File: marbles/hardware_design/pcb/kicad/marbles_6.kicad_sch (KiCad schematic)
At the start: 22 parts

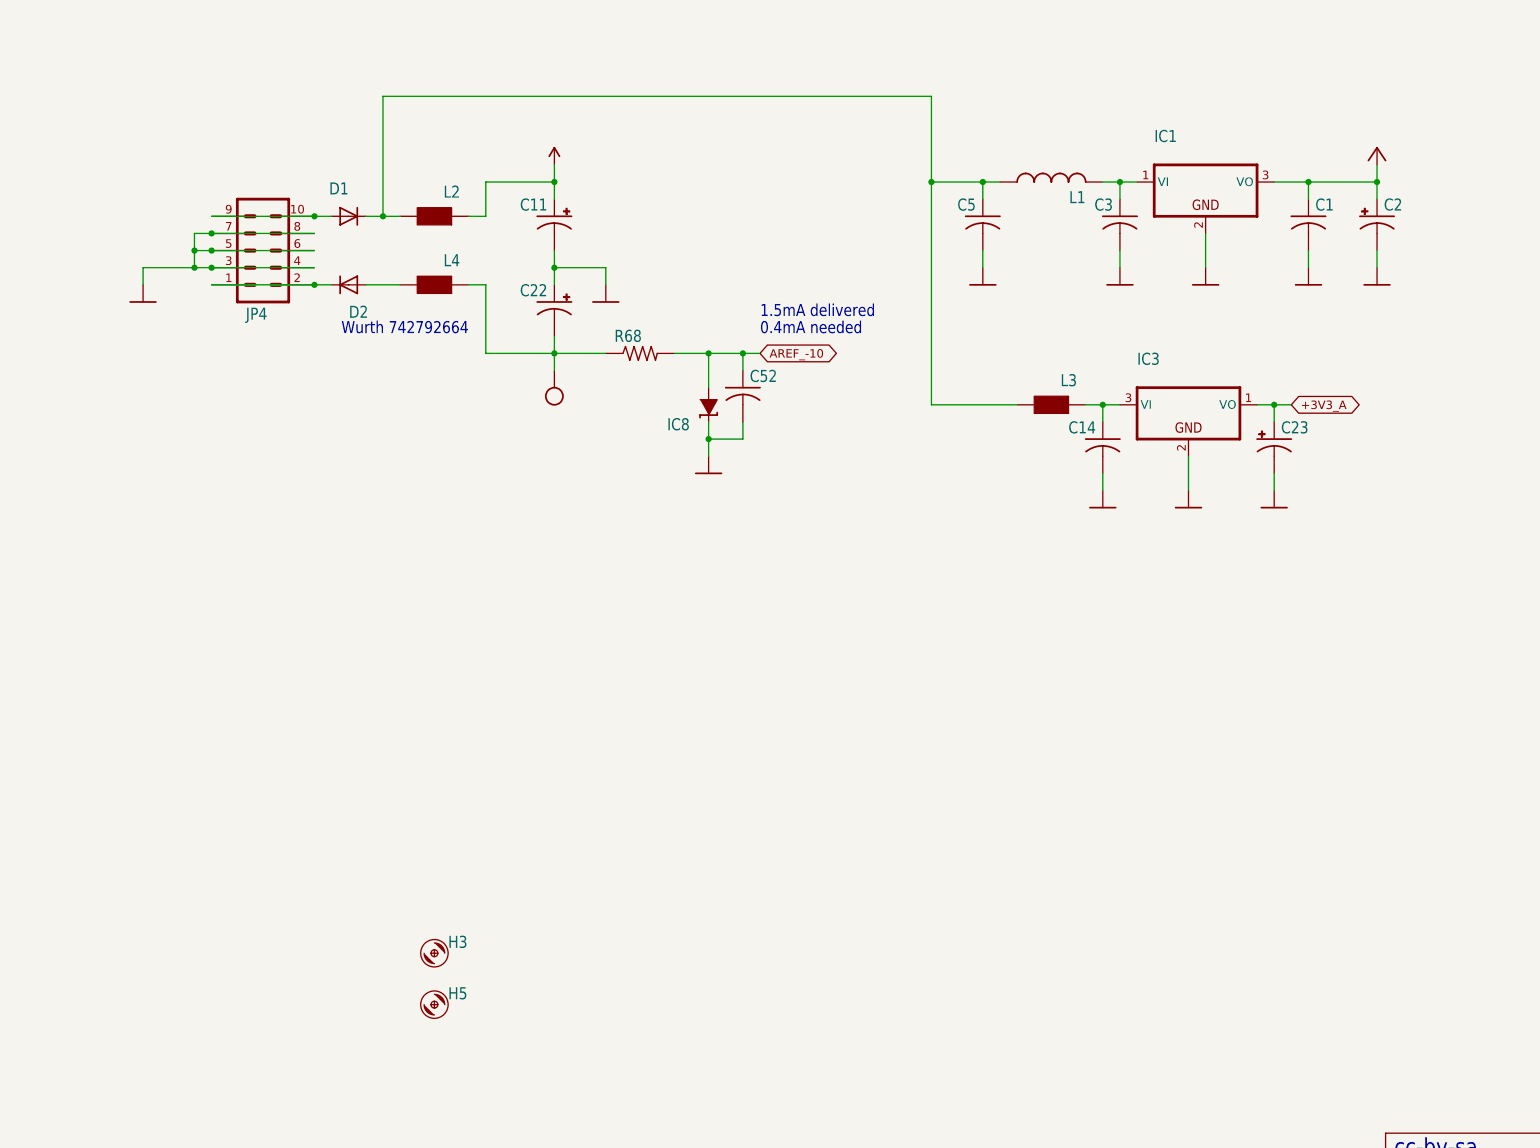
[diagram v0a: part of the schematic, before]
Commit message: added SMD LEDs in parallel with THT footprint
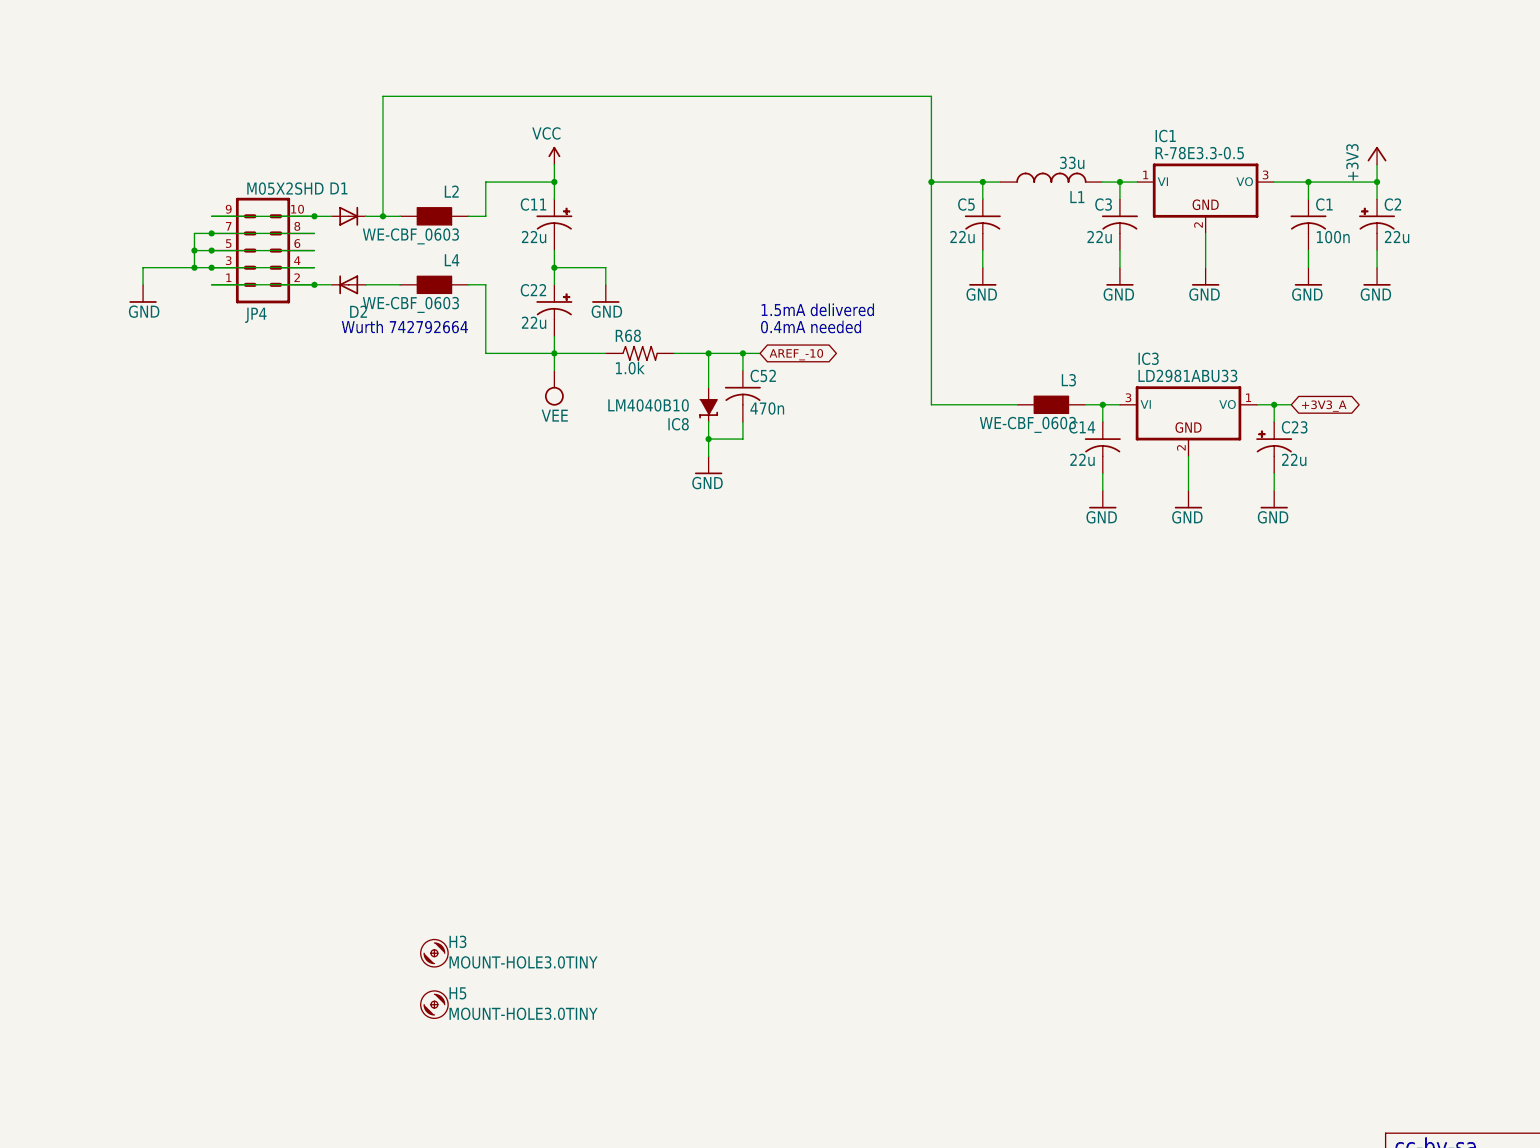
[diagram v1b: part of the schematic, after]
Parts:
- C1: value (none) -> 100n; footprint (none) -> marbles:C0402
- C11, C2, C22, C23: value (none) -> 22u; footprint (none) -> marbles:PANASONIC_C
- C14, C3, C5: value (none) -> 22u; footprint (none) -> marbles:C1206
- C52: value (none) -> 470n; footprint (none) -> marbles:C0402
- D1, D2: value (none) -> 1N5819HW; footprint (none) -> marbles:SOD123
- H3, H5: value (none) -> MOUNT-HOLE3.0TINY; footprint (none) -> marbles:3,0TINY
- IC1: value (none) -> R-78E3.3-0.5; footprint (none) -> marbles:WE78
- IC3: value (none) -> LD2981ABU33; footprint (none) -> marbles:SOT89
- IC8: value (none) -> LM4040B10; footprint (none) -> marbles:DBZ_R-PDSO-G3
- JP4: value (none) -> M05X2SHD; footprint (none) -> marbles:2X5-SHROUDED
- L1: value (none) -> 33u; footprint (none) -> marbles:L2012C
- L2, L3, L4: value (none) -> WE-CBF_0603; footprint (none) -> marbles:0603
- R68: value (none) -> 1.0k; footprint (none) -> marbles:R0402
